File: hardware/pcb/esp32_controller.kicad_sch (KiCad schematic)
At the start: 0 parts

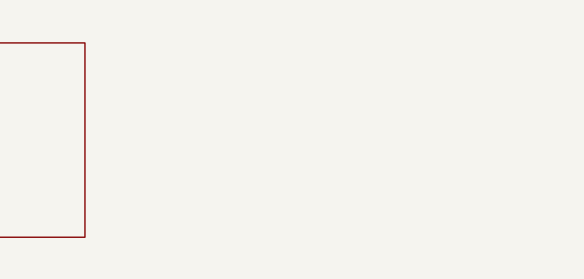
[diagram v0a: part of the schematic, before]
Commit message: draft: Added ESP32 and connector
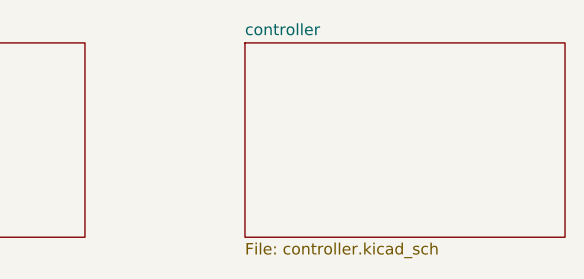
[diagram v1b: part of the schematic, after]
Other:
- added sheet controller (controller.kicad_sch)
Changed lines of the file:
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@@
 	(paper "A4")
+	(sheet
+		(at 120.65 45.72)
+		(size 35.56 21.59)
+		(fields_autoplaced yes)
+		(stroke
+			(width 0.1524)
+			(type solid)
+		)
+		(fill
+			(color 0 0 0 0.0000)
+		)
+		(property "Sheetname" "controller"
+			(at 120.65 45.0084 0)
+			(effects
+				(font
+					(size 1.27 1.27)
+				)
+				(justify left bottom)
+			)
+		)
+		(property "Sheetfile" "controller.kicad_sch"
+			(at 120.65 67.8946 0)
+			(effects
+				(font
+					(size 1.27 1.27)
+				)
+				(justify left top)
+			)
+		)
+		(instances
+			(project "esp32_controller"
+				(path "/3de317ca-1dad-48e6-a70d-ef8644bc7ddd"
+					(page "3")
+				)
+			)
+		)
+	)
 	(sheet
 		(at 67.31 45.72)

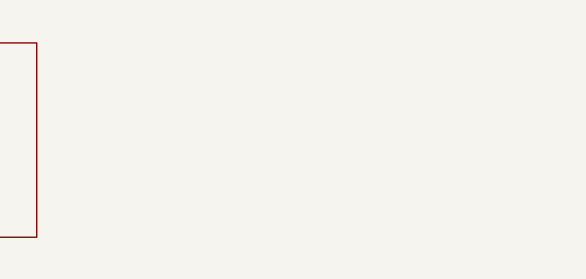
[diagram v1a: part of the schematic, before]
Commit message: draft: Added USB UART interface
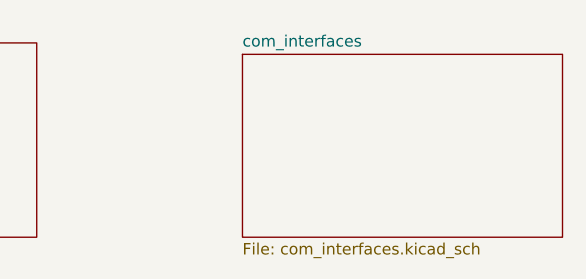
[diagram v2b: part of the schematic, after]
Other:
- added sheet com_interfaces (com_interfaces.kicad_sch)
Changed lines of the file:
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@@
+		)
+	)
+	(sheet
+		(at 179.07 46.99)
+		(size 35.56 20.32)
+		(fields_autoplaced yes)
+		(stroke
+			(width 0.1524)
+			(type solid)
+		)
+		(fill
+			(color 0 0 0 0.0000)
+		)
+		(property "Sheetname" "com_interfaces"
+			(at 179.07 46.2784 0)
+			(effects
+				(font
+					(size 1.27 1.27)
+				)
+				(justify left bottom)
+			)
+		)
+		(property "Sheetfile" "com_interfaces.kicad_sch"
+			(at 179.07 67.8946 0)
+			(effects
+				(font
+					(size 1.27 1.27)
+				)
+				(justify left top)
+			)
+		)
+		(instances
+			(project "esp32_controller"
+				(path "/3de317ca-1dad-48e6-a70d-ef8644bc7ddd"
+					(page "4")
+				)
+			)
 		)
 	)

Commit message: draft: High level overview
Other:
- note added: "High level overview"
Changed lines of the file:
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@@
 	(generator_version "8.0")
 	(paper "A4")
+	(text "High level overview"
+		(exclude_from_sim no)
+		(at 78.994 35.814 0)
+		(effects
+			(font
+				(size 2.54 2.54)
+				(thickness 0.508)
+				(bold yes)
+			)
+		)
+	)
 	(sheet
-		(at 120.65 45.72)
+		(at 114.3 115.57)
 		(size 35.56 21.59)
 		(fields_autoplaced yes)
@@
 		)
 		(property "Sheetname" "controller"
-			(at 120.65 45.0084 0)
+			(at 114.3 114.8584 0)
 			(effects
 				(font
@@
 		)
 		(property "Sheetfile" "controller.kicad_sch"
-			(at 120.65 67.8946 0)
+			(at 114.3 137.7446 0)
 			(effects
 				(font
@@
 	)
 	(sheet
-		(at 67.31 45.72)
+		(at 60.96 115.57)
 		(size 35.56 21.59)
 		(fields_autoplaced yes)
@@
 		)
 		(property "Sheetname" "power"
-			(at 67.31 45.0084 0)
+			(at 60.96 114.8584 0)
 			(effects
 				(font
@@
 		)
 		(property "Sheetfile" "power.kicad_sch"
-			(at 67.31 67.8946 0)
+			(at 60.96 137.7446 0)
 			(effects
 				(font
@@
 	)
 	(sheet
-		(at 179.07 46.99)
+		(at 172.72 116.84)
 		(size 35.56 20.32)
 		(fields_autoplaced yes)
@@
 		)
 		(property "Sheetname" "com_interfaces"
-			(at 179.07 46.2784 0)
+			(at 172.72 116.1284 0)
 			(effects
 				(font
@@
 		)
 		(property "Sheetfile" "com_interfaces.kicad_sch"
-			(at 179.07 67.8946 0)
+			(at 172.72 137.7446 0)
 			(effects
 				(font

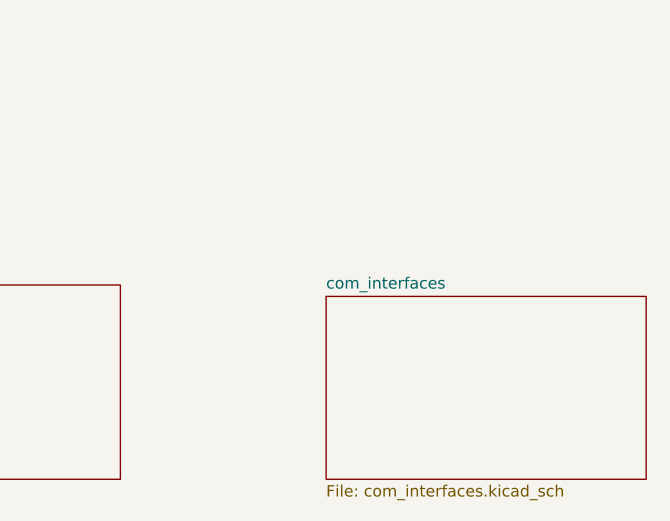
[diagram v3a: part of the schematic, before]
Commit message: draft: Added W5500 Ethernet
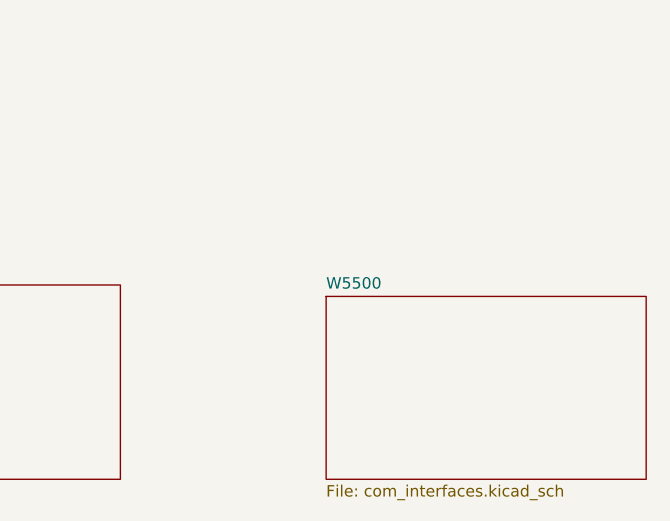
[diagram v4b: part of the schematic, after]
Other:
- sheet com_interfaces renamed W5500
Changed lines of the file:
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@@
 			(color 0 0 0 0.0000)
 		)
-		(property "Sheetname" "com_interfaces"
+		(property "Sheetname" "W5500"
 			(at 172.72 116.1284 0)
 			(effects
